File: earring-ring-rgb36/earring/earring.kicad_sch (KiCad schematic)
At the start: 44 parts, among them J1 Conn_01x04, SW1 SW_Push, U2 STM32L031G6Ux

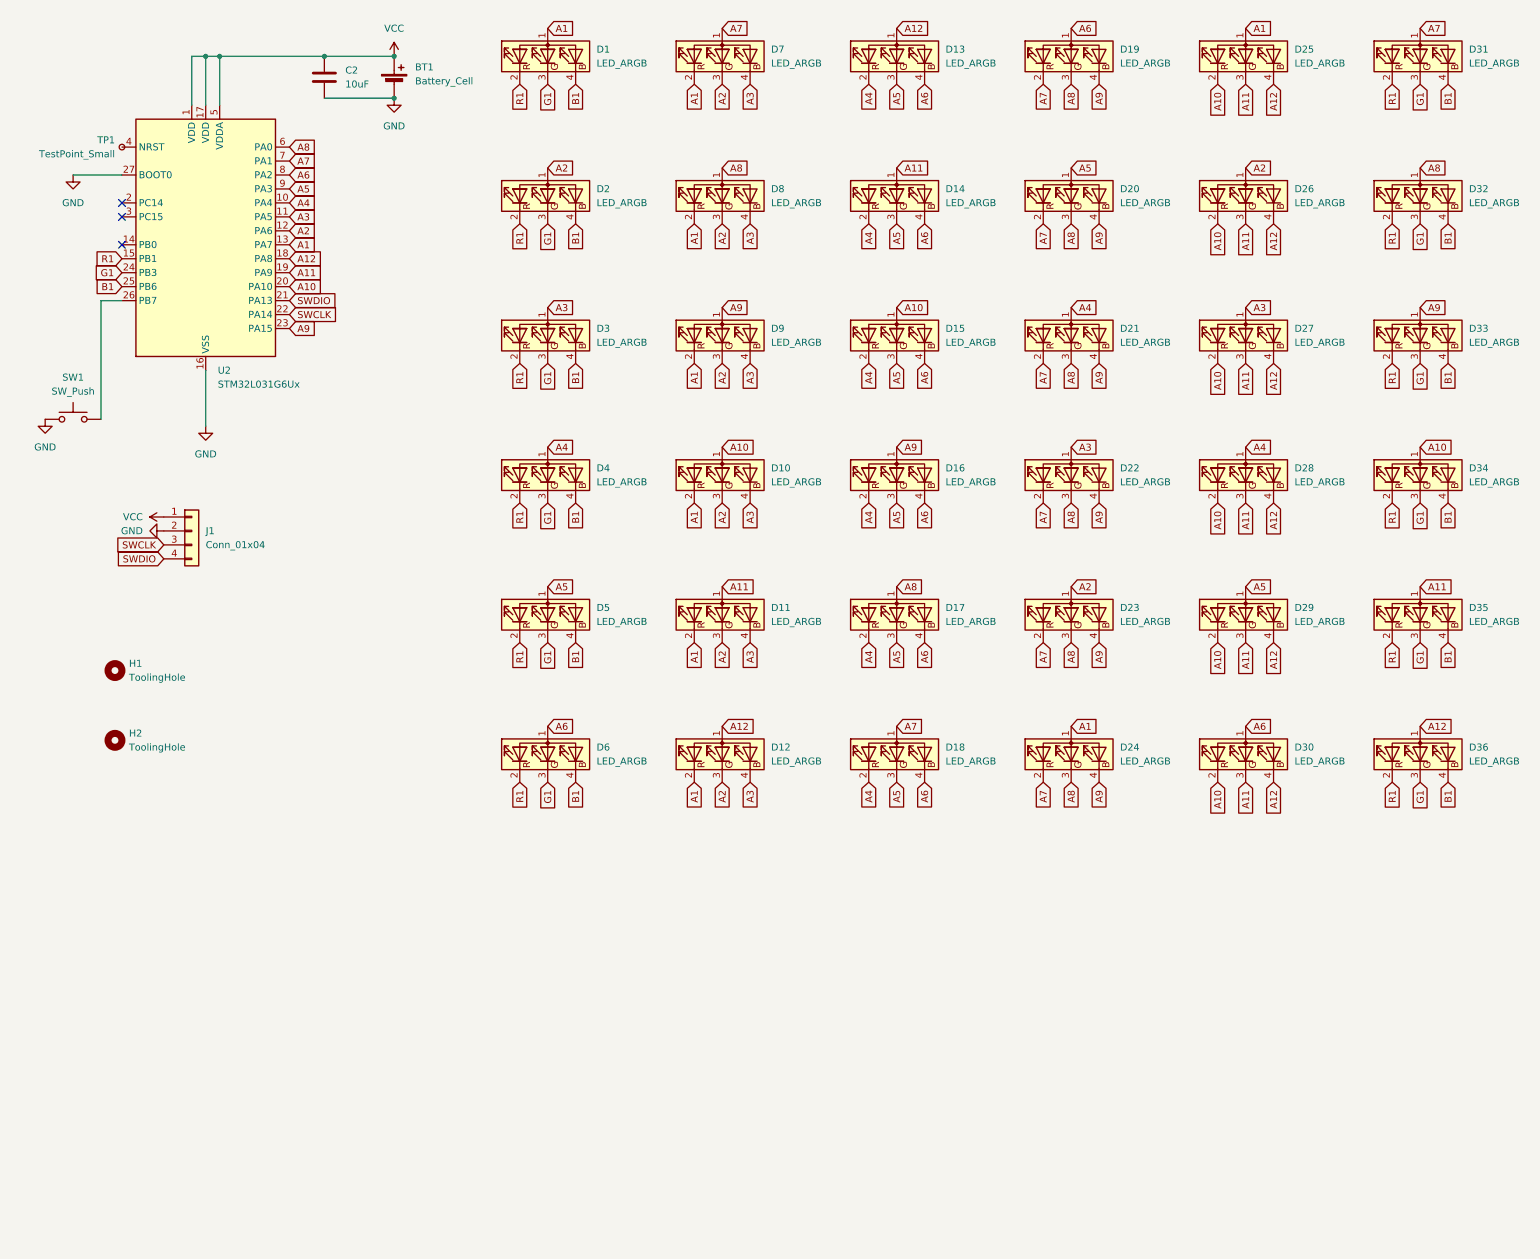
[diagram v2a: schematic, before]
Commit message: earring-ring-rgb36: completely redid the schematic/PCB
Use 9x4 instead of 6x6 rows of LEDs. This should be more efficient to
control in software and actually simplifies the PCB a lot.

I also redid the routing of the PCB entirely:

  * Sit closer to the JLCPCB trace distance limit. Now most traces are
    0.2mm wide with 0.1mm spacing, whereas the limit is 0.10mm/0.10mm.
  * Put *two* traces between the LEDs. This simplifies the layout
    massively.
  * Switch to a two-layer board. We don't need the middle layers
    anymore with the above simplifications. This should make things
    cheaper and offer more options regarding color etc.
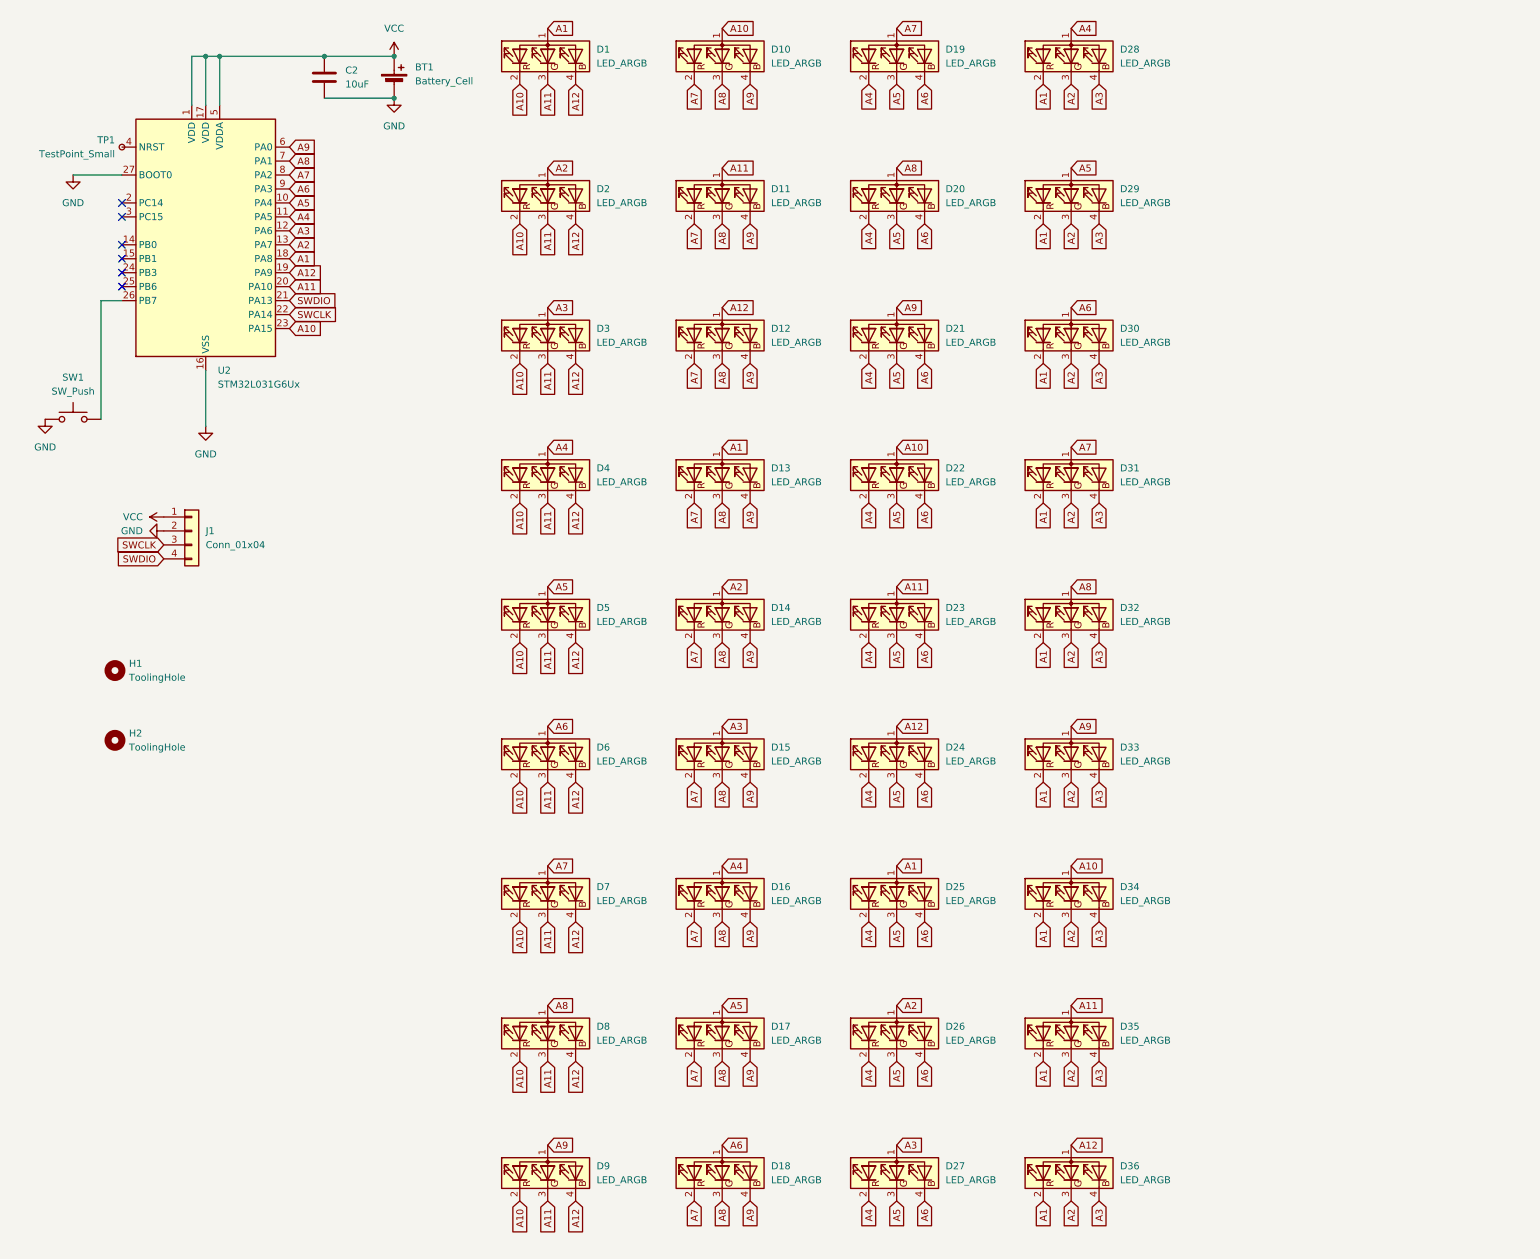
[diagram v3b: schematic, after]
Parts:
- TP1: now left out of the parts list
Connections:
- net A1: now also D13.1 (A), D28.2 (RK), D29.2 (RK), D30.2 (RK), D31.2 (RK), D32.2 (RK), D33.2 (RK), D34.2 (RK), D35.2 (RK), D36.2 (RK), U2.18 (PA8); no longer D10.2 (RK), D11.2 (RK), D12.2 (RK), D24.1 (A), D7.2 (RK), D8.2 (RK), D9.2 (RK), U2.13 (PA7)
- net A10: now also D1.2 (RK), D2.2 (RK), D22.1 (A), D3.2 (RK), D4.2 (RK), D5.2 (RK), D6.2 (RK), D7.2 (RK), D8.2 (RK), D9.2 (RK), U2.23 (PA15); no longer D15.1 (A), D25.2 (RK), D26.2 (RK), D27.2 (RK), D28.2 (RK), D29.2 (RK), D30.2 (RK), U2.20 (PA10)
- net A11: now also D1.3 (GK), D2.3 (GK), D23.1 (A), D3.3 (GK), D4.3 (GK), D5.3 (GK), D6.3 (GK), D7.3 (GK), D8.3 (GK), D9.3 (GK), U2.20 (PA10); no longer D14.1 (A), D25.3 (GK), D26.3 (GK), D27.3 (GK), D28.3 (GK), D29.3 (GK), D30.3 (GK), U2.19 (PA9)
- net A12: now also D1.4 (BK), D2.4 (BK), D24.1 (A), D3.4 (BK), D4.4 (BK), D5.4 (BK), D6.4 (BK), D7.4 (BK), D8.4 (BK), D9.4 (BK), U2.19 (PA9); no longer D13.1 (A), D25.4 (BK), D26.4 (BK), D27.4 (BK), D28.4 (BK), D29.4 (BK), D30.4 (BK), U2.18 (PA8)
- net A2: now also D14.1 (A), D28.3 (GK), D29.3 (GK), D30.3 (GK), D31.3 (GK), D32.3 (GK), D33.3 (GK), D34.3 (GK), D35.3 (GK), D36.3 (GK), U2.13 (PA7); no longer D10.3 (GK), D11.3 (GK), D12.3 (GK), D23.1 (A), D7.3 (GK), D8.3 (GK), D9.3 (GK), U2.12 (PA6)
- net A3: now also D15.1 (A), D28.4 (BK), D29.4 (BK), D30.4 (BK), D31.4 (BK), D32.4 (BK), D33.4 (BK), D34.4 (BK), D35.4 (BK), D36.4 (BK), U2.12 (PA6); no longer D10.4 (BK), D11.4 (BK), D12.4 (BK), D22.1 (A), D7.4 (BK), D8.4 (BK), D9.4 (BK), U2.11 (PA5)
- net A4: now also D16.1 (A), D19.2 (RK), D20.2 (RK), D21.2 (RK), D22.2 (RK), D23.2 (RK), D24.2 (RK), D25.2 (RK), D26.2 (RK), D27.2 (RK), U2.11 (PA5); no longer D13.2 (RK), D14.2 (RK), D15.2 (RK), D16.2 (RK), D17.2 (RK), D18.2 (RK), D21.1 (A), U2.10 (PA4)
- net A5: now also D17.1 (A), D19.3 (GK), D20.3 (GK), D21.3 (GK), D22.3 (GK), D23.3 (GK), D24.3 (GK), D25.3 (GK), D26.3 (GK), D27.3 (GK), U2.10 (PA4); no longer D13.3 (GK), D14.3 (GK), D15.3 (GK), D16.3 (GK), D17.3 (GK), D18.3 (GK), D20.1 (A), U2.9 (PA3)
- net A6: now also D18.1 (A), D19.4 (BK), D20.4 (BK), D21.4 (BK), D22.4 (BK), D23.4 (BK), D24.4 (BK), D25.4 (BK), D26.4 (BK), D27.4 (BK), U2.9 (PA3); no longer D13.4 (BK), D14.4 (BK), D15.4 (BK), D16.4 (BK), D17.4 (BK), D18.4 (BK), D19.1 (A), U2.8 (PA2)
- net A7: now also D10.2 (RK), D11.2 (RK), D12.2 (RK), D13.2 (RK), D14.2 (RK), D15.2 (RK), D16.2 (RK), D17.2 (RK), D18.2 (RK), D19.1 (A), U2.8 (PA2); no longer D18.1 (A), D19.2 (RK), D20.2 (RK), D21.2 (RK), D22.2 (RK), D23.2 (RK), D24.2 (RK), U2.7 (PA1)
- net A8: now also D10.3 (GK), D11.3 (GK), D12.3 (GK), D13.3 (GK), D14.3 (GK), D15.3 (GK), D16.3 (GK), D17.3 (GK), D18.3 (GK), D20.1 (A), U2.7 (PA1); no longer D17.1 (A), D19.3 (GK), D20.3 (GK), D21.3 (GK), D22.3 (GK), D23.3 (GK), D24.3 (GK), U2.6 (PA0)
- net A9: now also D10.4 (BK), D11.4 (BK), D12.4 (BK), D13.4 (BK), D14.4 (BK), D15.4 (BK), D16.4 (BK), D17.4 (BK), D18.4 (BK), D21.1 (A), U2.6 (PA0); no longer D16.1 (A), D19.4 (BK), D20.4 (BK), D21.4 (BK), D22.4 (BK), D23.4 (BK), D24.4 (BK), U2.23 (PA15)
- removed net B1: D1.4 (BK), D2.4 (BK), D3.4 (BK), D31.4 (BK), D32.4 (BK), D33.4 (BK), D34.4 (BK), D35.4 (BK), D36.4 (BK), D4.4 (BK), D5.4 (BK), D6.4 (BK), U2.25 (PB6)
- removed net G1: D1.3 (GK), D2.3 (GK), D3.3 (GK), D31.3 (GK), D32.3 (GK), D33.3 (GK), D34.3 (GK), D35.3 (GK), D36.3 (GK), D4.3 (GK), D5.3 (GK), D6.3 (GK), U2.24 (PB3)
- removed net R1: D1.2 (RK), D2.2 (RK), D3.2 (RK), D31.2 (RK), D32.2 (RK), D33.2 (RK), D34.2 (RK), D35.2 (RK), D36.2 (RK), D4.2 (RK), D5.2 (RK), D6.2 (RK), U2.15 (PB1)
- no-connect marks 3 -> 6
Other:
- moved on the sheet: D10, D11, D12, D13, D14, D15, D16, D17, D18, D19, D20, D21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

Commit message: earring-ring-rgb36: rotate net names so the labels make a bit more sense
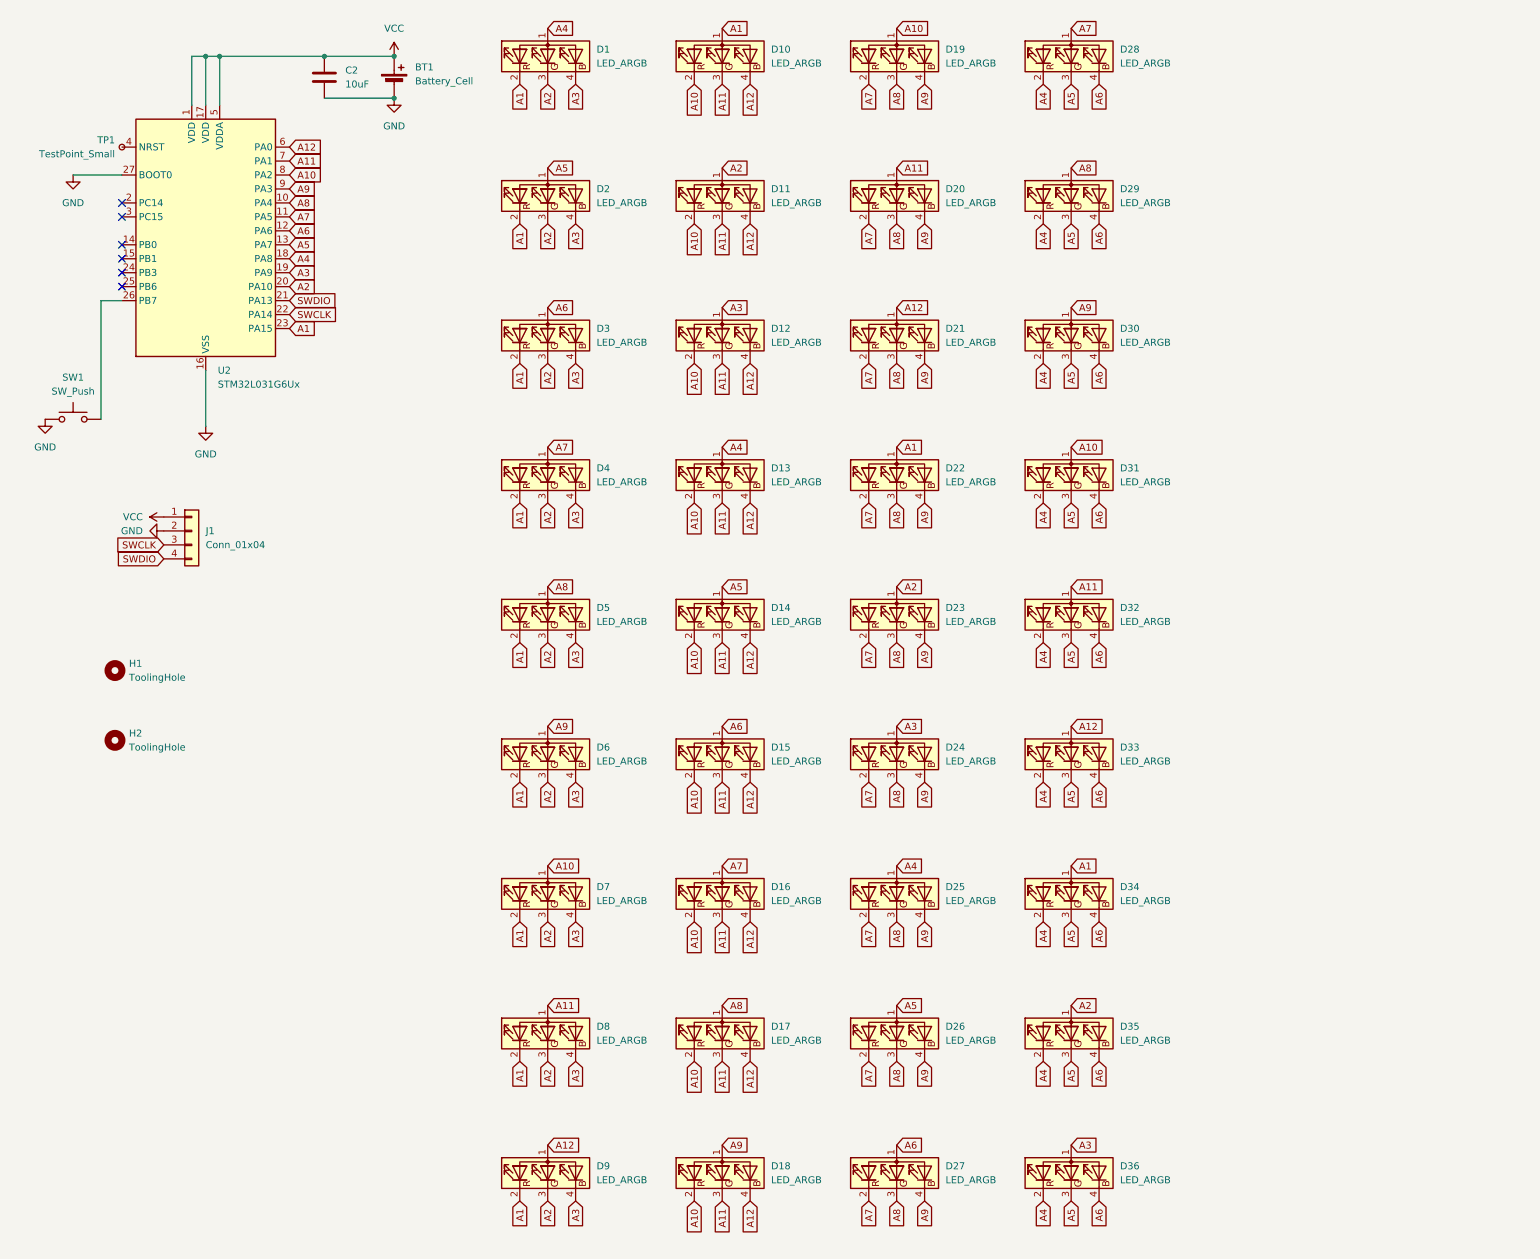
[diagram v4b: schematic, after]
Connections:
- net A1: now also D1.2 (RK), D10.1 (A), D2.2 (RK), D22.1 (A), D3.2 (RK), D34.1 (A), D4.2 (RK), D5.2 (RK), D6.2 (RK), D7.2 (RK), D8.2 (RK), D9.2 (RK), U2.23 (PA15); no longer D1.1 (A), D13.1 (A), D25.1 (A), D28.2 (RK), D29.2 (RK), D30.2 (RK), D31.2 (RK), D32.2 (RK), D33.2 (RK), D34.2 (RK), D35.2 (RK), D36.2 (RK), U2.18 (PA8)
- net A10: now also D10.2 (RK), D11.2 (RK), D12.2 (RK), D13.2 (RK), D14.2 (RK), D15.2 (RK), D16.2 (RK), D17.2 (RK), D18.2 (RK), D19.1 (A), D31.1 (A), D7.1 (A), U2.8 (PA2); no longer D1.2 (RK), D10.1 (A), D2.2 (RK), D22.1 (A), D3.2 (RK), D34.1 (A), D4.2 (RK), D5.2 (RK), D6.2 (RK), D7.2 (RK), D8.2 (RK), D9.2 (RK), U2.23 (PA15)
- net A11: now also D10.3 (GK), D11.3 (GK), D12.3 (GK), D13.3 (GK), D14.3 (GK), D15.3 (GK), D16.3 (GK), D17.3 (GK), D18.3 (GK), D20.1 (A), D32.1 (A), D8.1 (A), U2.7 (PA1); no longer D1.3 (GK), D11.1 (A), D2.3 (GK), D23.1 (A), D3.3 (GK), D35.1 (A), D4.3 (GK), D5.3 (GK), D6.3 (GK), D7.3 (GK), D8.3 (GK), D9.3 (GK), U2.20 (PA10)
- net A12: now also D10.4 (BK), D11.4 (BK), D12.4 (BK), D13.4 (BK), D14.4 (BK), D15.4 (BK), D16.4 (BK), D17.4 (BK), D18.4 (BK), D21.1 (A), D33.1 (A), D9.1 (A), U2.6 (PA0); no longer D1.4 (BK), D12.1 (A), D2.4 (BK), D24.1 (A), D3.4 (BK), D36.1 (A), D4.4 (BK), D5.4 (BK), D6.4 (BK), D7.4 (BK), D8.4 (BK), D9.4 (BK), U2.19 (PA9)
- net A2: now also D1.3 (GK), D11.1 (A), D2.3 (GK), D23.1 (A), D3.3 (GK), D35.1 (A), D4.3 (GK), D5.3 (GK), D6.3 (GK), D7.3 (GK), D8.3 (GK), D9.3 (GK), U2.20 (PA10); no longer D14.1 (A), D2.1 (A), D26.1 (A), D28.3 (GK), D29.3 (GK), D30.3 (GK), D31.3 (GK), D32.3 (GK), D33.3 (GK), D34.3 (GK), D35.3 (GK), D36.3 (GK), U2.13 (PA7)
- net A3: now also D1.4 (BK), D12.1 (A), D2.4 (BK), D24.1 (A), D3.4 (BK), D36.1 (A), D4.4 (BK), D5.4 (BK), D6.4 (BK), D7.4 (BK), D8.4 (BK), D9.4 (BK), U2.19 (PA9); no longer D15.1 (A), D27.1 (A), D28.4 (BK), D29.4 (BK), D3.1 (A), D30.4 (BK), D31.4 (BK), D32.4 (BK), D33.4 (BK), D34.4 (BK), D35.4 (BK), D36.4 (BK), U2.12 (PA6)
- net A4: now also D1.1 (A), D13.1 (A), D25.1 (A), D28.2 (RK), D29.2 (RK), D30.2 (RK), D31.2 (RK), D32.2 (RK), D33.2 (RK), D34.2 (RK), D35.2 (RK), D36.2 (RK), U2.18 (PA8); no longer D16.1 (A), D19.2 (RK), D20.2 (RK), D21.2 (RK), D22.2 (RK), D23.2 (RK), D24.2 (RK), D25.2 (RK), D26.2 (RK), D27.2 (RK), D28.1 (A), D4.1 (A), U2.11 (PA5)
- net A5: now also D14.1 (A), D2.1 (A), D26.1 (A), D28.3 (GK), D29.3 (GK), D30.3 (GK), D31.3 (GK), D32.3 (GK), D33.3 (GK), D34.3 (GK), D35.3 (GK), D36.3 (GK), U2.13 (PA7); no longer D17.1 (A), D19.3 (GK), D20.3 (GK), D21.3 (GK), D22.3 (GK), D23.3 (GK), D24.3 (GK), D25.3 (GK), D26.3 (GK), D27.3 (GK), D29.1 (A), D5.1 (A), U2.10 (PA4)
- net A6: now also D15.1 (A), D27.1 (A), D28.4 (BK), D29.4 (BK), D3.1 (A), D30.4 (BK), D31.4 (BK), D32.4 (BK), D33.4 (BK), D34.4 (BK), D35.4 (BK), D36.4 (BK), U2.12 (PA6); no longer D18.1 (A), D19.4 (BK), D20.4 (BK), D21.4 (BK), D22.4 (BK), D23.4 (BK), D24.4 (BK), D25.4 (BK), D26.4 (BK), D27.4 (BK), D30.1 (A), D6.1 (A), U2.9 (PA3)
- net A7: now also D16.1 (A), D19.2 (RK), D20.2 (RK), D21.2 (RK), D22.2 (RK), D23.2 (RK), D24.2 (RK), D25.2 (RK), D26.2 (RK), D27.2 (RK), D28.1 (A), D4.1 (A), U2.11 (PA5); no longer D10.2 (RK), D11.2 (RK), D12.2 (RK), D13.2 (RK), D14.2 (RK), D15.2 (RK), D16.2 (RK), D17.2 (RK), D18.2 (RK), D19.1 (A), D31.1 (A), D7.1 (A), U2.8 (PA2)
- net A8: now also D17.1 (A), D19.3 (GK), D20.3 (GK), D21.3 (GK), D22.3 (GK), D23.3 (GK), D24.3 (GK), D25.3 (GK), D26.3 (GK), D27.3 (GK), D29.1 (A), D5.1 (A), U2.10 (PA4); no longer D10.3 (GK), D11.3 (GK), D12.3 (GK), D13.3 (GK), D14.3 (GK), D15.3 (GK), D16.3 (GK), D17.3 (GK), D18.3 (GK), D20.1 (A), D32.1 (A), D8.1 (A), U2.7 (PA1)
- net A9: now also D18.1 (A), D19.4 (BK), D20.4 (BK), D21.4 (BK), D22.4 (BK), D23.4 (BK), D24.4 (BK), D25.4 (BK), D26.4 (BK), D27.4 (BK), D30.1 (A), D6.1 (A), U2.9 (PA3); no longer D10.4 (BK), D11.4 (BK), D12.4 (BK), D13.4 (BK), D14.4 (BK), D15.4 (BK), D16.4 (BK), D17.4 (BK), D18.4 (BK), D21.1 (A), D33.1 (A), D9.1 (A), U2.6 (PA0)
